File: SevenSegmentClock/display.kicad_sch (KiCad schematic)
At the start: 86 parts, among them Q1 PN2222A, Q2 PN2222A, Q3 PN2222A, Q4 PN2222A, U1 4504, U10 4511, U2 74HC138, U3 4504, U4 4042, U5 4511, U6 4511, U7 4511, U8 4511, U9 4511

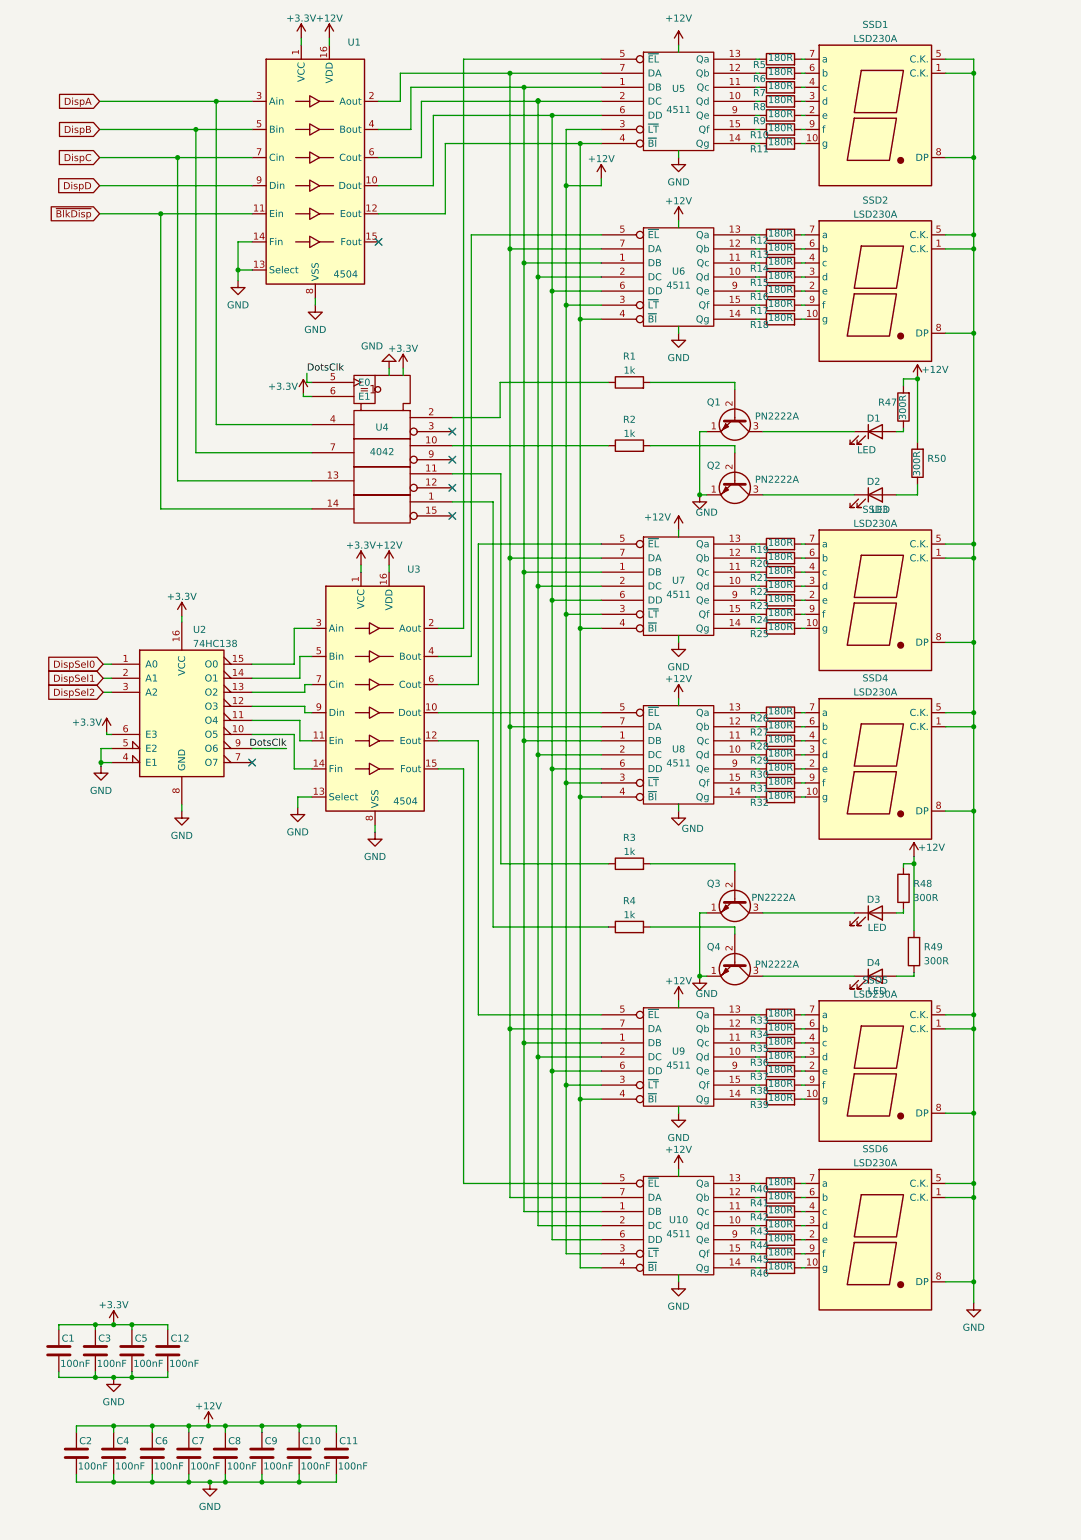
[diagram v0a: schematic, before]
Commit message: Using SigmaDelta to implement dimming of the display
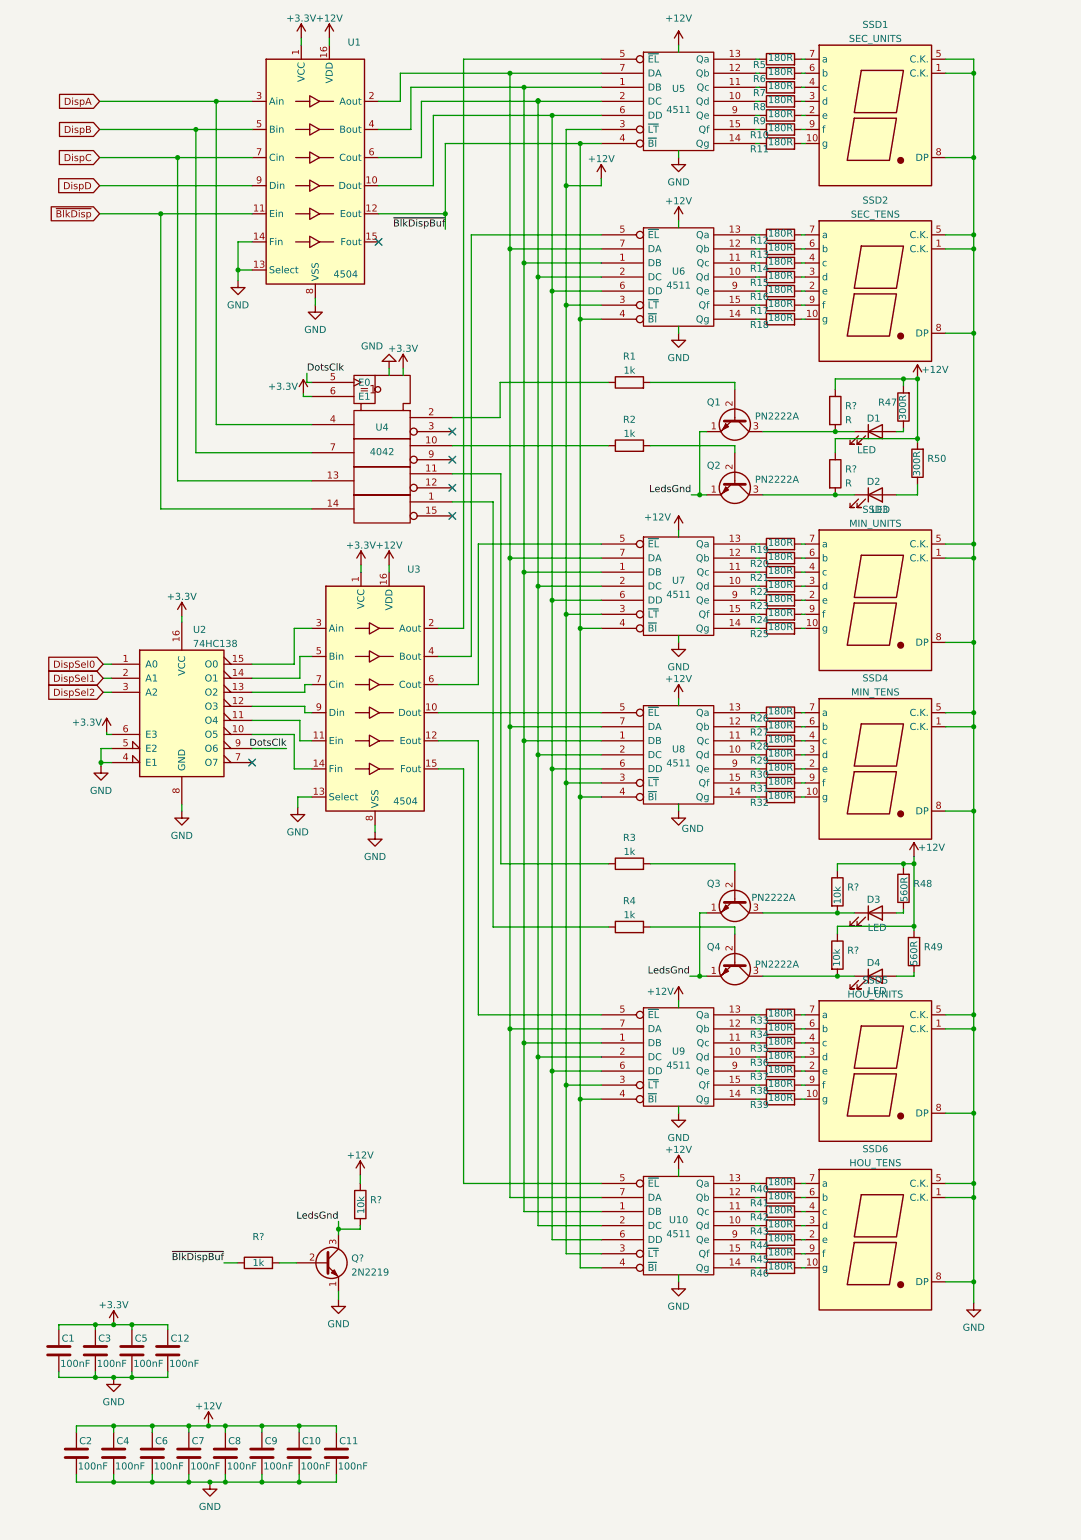
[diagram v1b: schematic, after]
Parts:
- added Q?: 2N2219, Package_TO_SOT_THT:TO-39-3, symbol Transistor_BJT:2N2219
- added R? (x3): 10k, symbol Device:R
- added R? (x2): R, symbol Device:R
- added R?: 1k, symbol Device:R
- R48, R49: value 300R -> 560R
- SSD1: value LSD230A -> SEC_UNITS
- SSD2: value LSD230A -> SEC_TENS
- SSD3: value LSD230A -> MIN_UNITS
- SSD4: value LSD230A -> MIN_TENS
- SSD5: value LSD230A -> HOU_UNITS
- SSD6: value LSD230A -> HOU_TENS
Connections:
- net +12V: now also R?.1, R?.1, R?.1, R?.1, R?.1
- net GND: now also Q?.1 (E); no longer Q1.1 (E), Q2.1 (E), Q3.1 (E), Q4.1 (E)
- net at D2.1 (K), Q2.3 (C): now also R?.2
- net at D1.1 (K), Q1.3 (C): now also R?.2
- net at D3.1 (K), Q3.3 (C): now also R?.2
- net ~{BlkDispBuf}: now reaches U1.12 (Eout), U10.4 (~{BI}), U5.4 (~{BI}), U6.4 (~{BI}), U7.4 (~{BI}), U8.4 (~{BI}), U9.4 (~{BI})
- net ~{BlkDispBuf}: now also R?.1
- net at D4.1 (K), Q4.3 (C): now also R?.2
- new net: Q?.2 (B), R?.2
- new net LedsGnd: Q1.1 (E), Q2.1 (E), Q3.1 (E), Q4.1 (E), Q?.3 (C), R?.2

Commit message: Adding two more displays to show a degree and a percent symbols
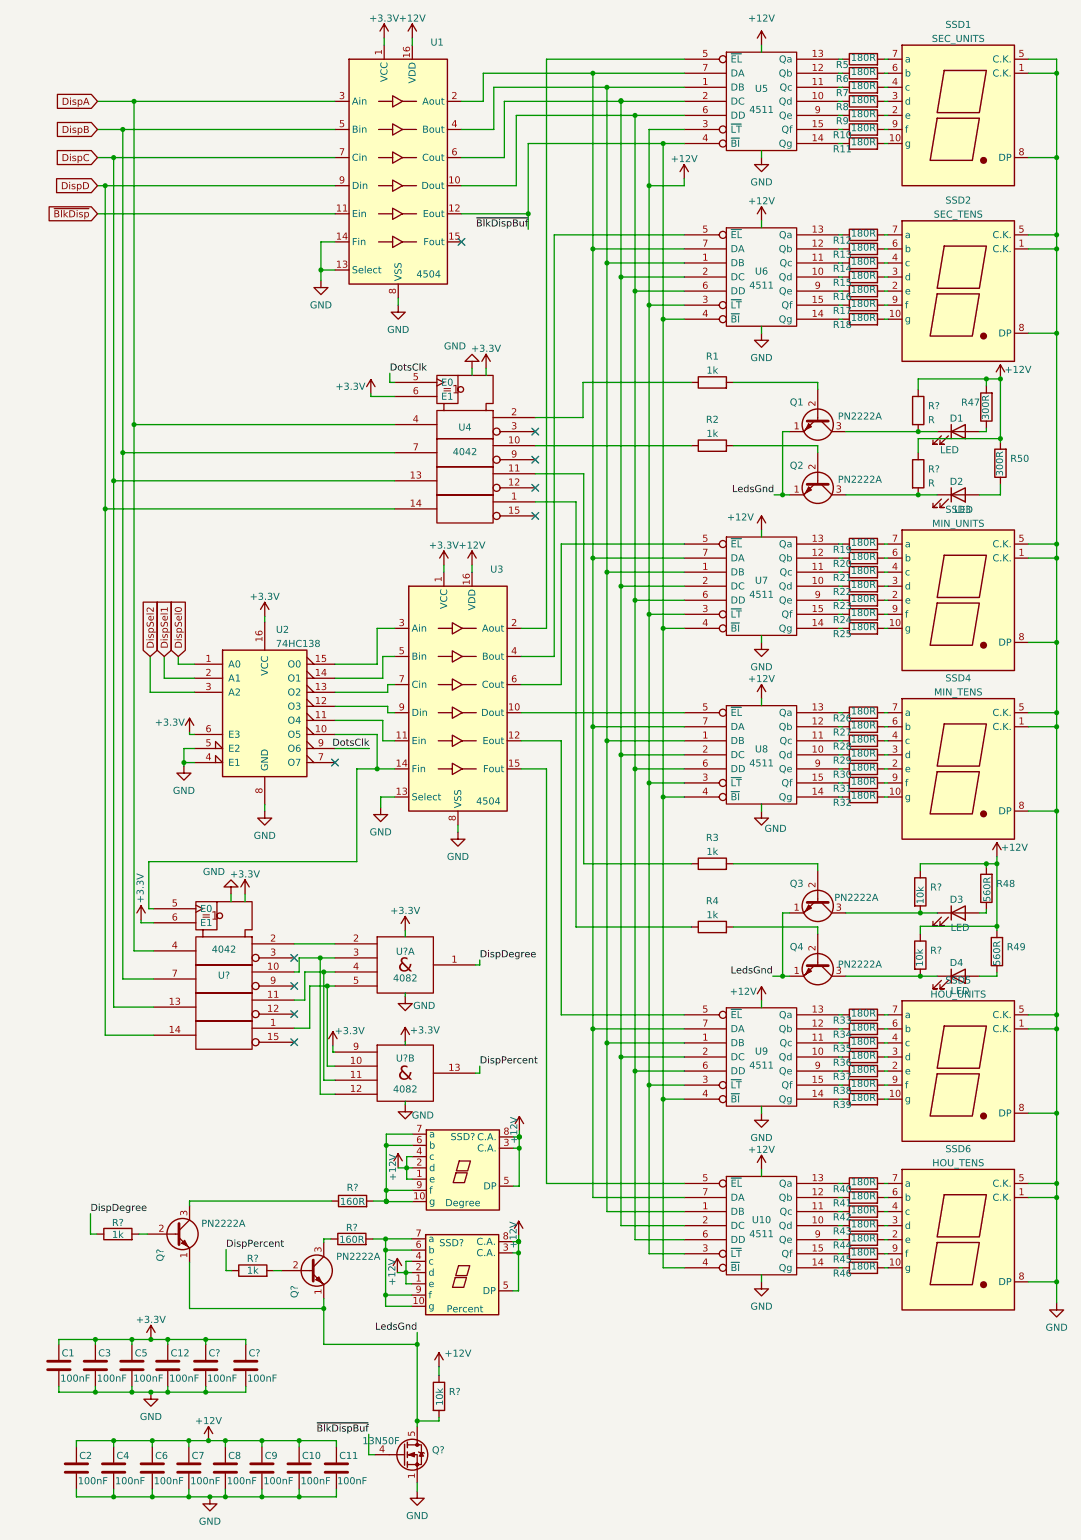
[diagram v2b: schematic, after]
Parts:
- removed Q?: 2N2219, Package_TO_SOT_THT:TO-39-3, symbol Transistor_BJT:2N2219
- removed R?: 1k, symbol Device:R
- added C? (x2): 100nF, Capacitor_THT:C_Disc_D5.0mm_W2.5mm_P5.00mm, symbol Device:C
- added Q? (x2): PN2222A, Package_TO_SOT_THT:TO-92_Inline, symbol Transistor_BJT:PN2222A
- added Q?: 13N50F, Package_TO_SOT_SMD:LFPAK33, symbol Transistor_FET:BUK7M67-60EX
- added R? (x2): 1k, symbol Device:R
- added R? (x2): 160R, symbol Device:R
- added SSD?: Degree, symbol Library:WCN1-1056
- added SSD?: Percent, symbol Library:WCN1-1056
- added U? (x2): 4082, symbol 4xxx_IEEE:4082
- added U?: 4042, symbol 4xxx_IEEE:4042
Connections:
- net +12V: now also C?.1, C?.1, SSD?.1 (e), SSD?.1 (e), SSD?.2 (d), SSD?.2 (d), SSD?.3 (C.A.), SSD?.3 (C.A.), SSD?.4 (c), SSD?.4 (c), SSD?.5 (DP), SSD?.5 (DP), SSD?.8 (C.A.), SSD?.8 (C.A.), U?.14 (Vdd), U?.14 (Vdd), U?.16 (Vdd), U?.6 (E1), U?.9
- net DispA: now also U?.4
- net DispB: now also U?.7
- net DispC: now also U?.13
- net DispD: now also U4.14, U?.14
- net GND: now also C?.2, C?.2, Q?.1 (S), Q?.2 (S), Q?.3 (S), U?.7 (Vss), U?.7 (Vss), U?.8 (Vss)
- net LedsGnd: now also Q?.1 (E), Q?.1 (E), Q?.5 (D)
- net ~{BlkDispBuf}: now also Q?.4 (G)
- net ~{BlkDisp}: no longer U4.14
- net at U2.10 (O5), U3.14 (Fin): now also U?.5 (E0)
- new net: U?.2, U?.2
- new net: U?.10, U?.12, U?.3
- new net: U?.11, U?.11, U?.4
- new net: U?.1, U?.10, U?.5
- new net: Q?.2 (B), R?.2 (x2)
- new net: Q?.3 (C), R?.1 (x2)
- new net: R?.2, SSD?.10 (g), SSD?.6 (b), SSD?.7 (a), SSD?.9 (f) (x2)
- new net DispDegree: R?.1, U?.1
- new net DispPercent: R?.1, U?.13
- no-connect marks 6 -> 10
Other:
- moved on the sheet: C1, C10, C11, C12, C2, C3, C4, C5, C6, C7, C8, C9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

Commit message: Adding the control schematic and fixing Eletrical Rules Checks
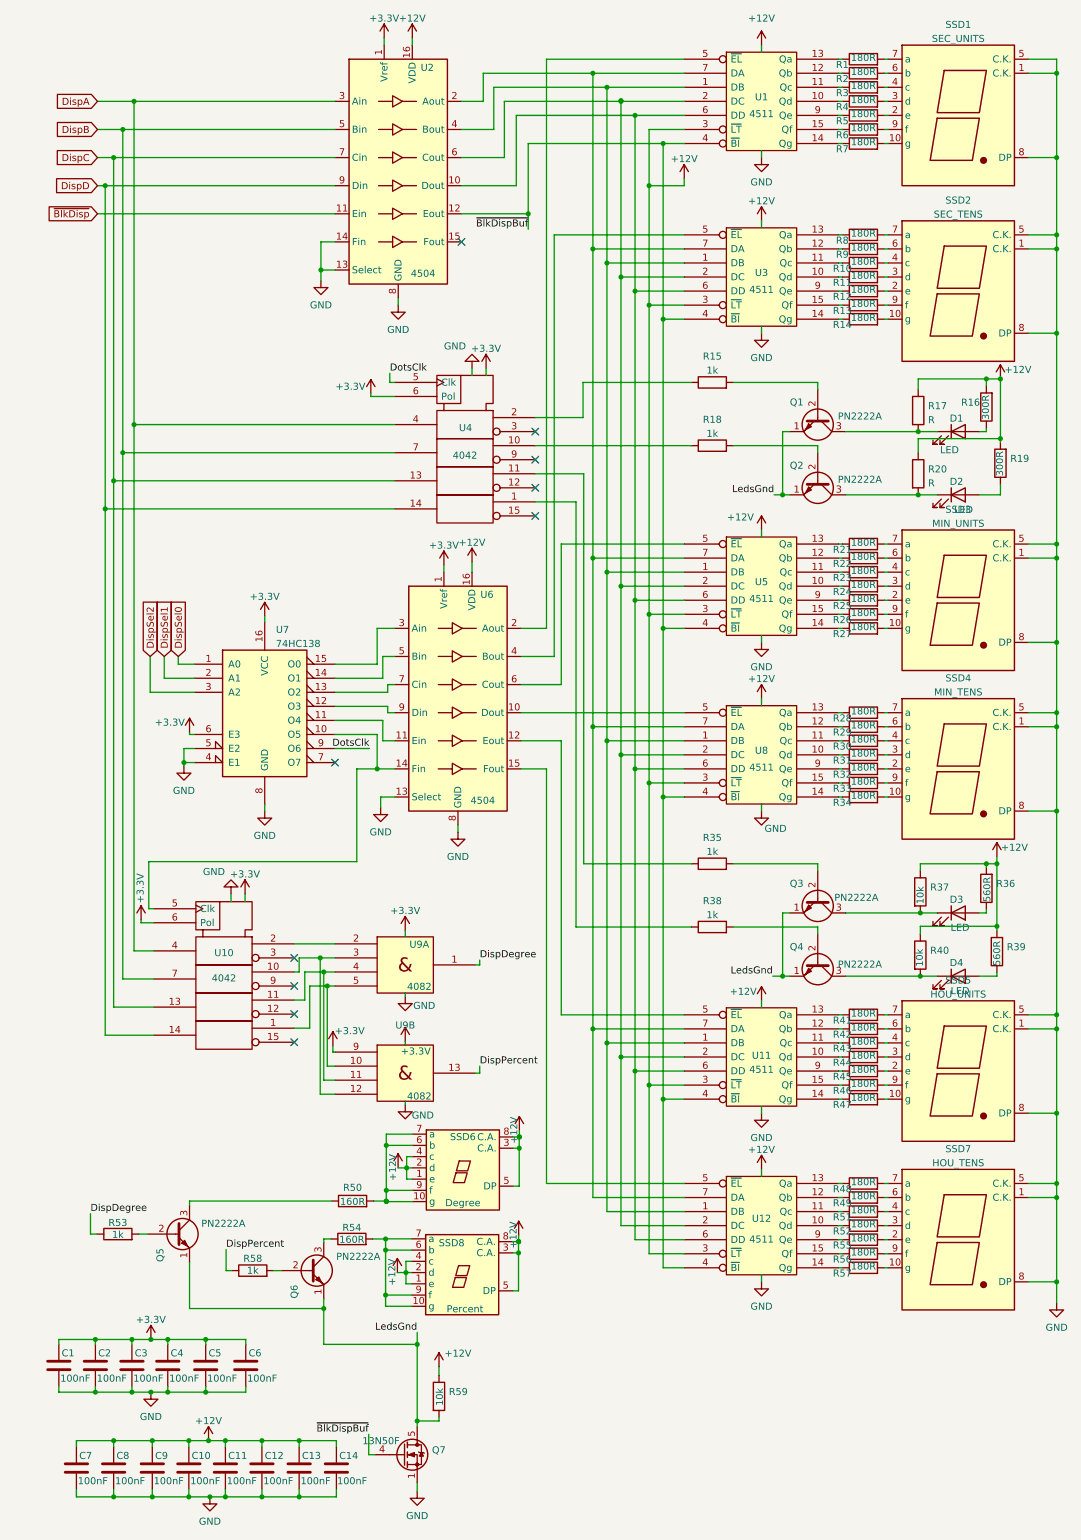
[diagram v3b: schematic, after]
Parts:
- removed U1, U3: 4504, Package_SO:SOIC-16_3.9x9.9mm_P1.27mm, symbol 4xxx:4504
- removed U10, U5, U6, U7, U8, U9: 4511, Package_SO:SOIC-16_3.9x9.9mm_P1.27mm, symbol 4xxx_IEEE:4511
- removed U4: 4042, Package_DIP:DIP-16_W7.62mm_LongPads, symbol 4xxx_IEEE:4042
- removed U? (x2): 4082, symbol 4xxx_IEEE:4082
- removed U?: 4042, symbol 4xxx_IEEE:4042
- added U1, U11, U12, U3, U5, U8: 4511, symbol Library:4511
- added U10, U4: 4042, symbol Library:4042
- added U2, U6: 4504, symbol Library:4504
- added U9: 4082, symbol Library:4082
- gave numbers to parts that had none: 16
- renumbered C7 to C10, C8 to C11, C9 to C12, C10 to C13, C11 to C14, C3 to C2, C5 to C3, C12 to C4, C2 to C7, C4 to C8, C6 to C9, R5 to R1, R14 to R10, R15 to R11, R16 to R12, R17 to R13, R18 to R14, R1 to R15, R47 to R16, R2 to R18, R50 to R19, R6 to R2, R19 to R21, R20 to R22, R21 to R23, R22 to R24, R23 to R25, R24 to R26, R25 to R27, R26 to R28, R27 to R29, R7 to R3, R28 to R30, R29 to R31, R30 to R32, R31 to R33, R32 to R34, R3 to R35, R48 to R36, R4 to R38, R49 to R39, R8 to R4, R33 to R41, R34 to R42, R35 to R43, R36 to R44, R37 to R45, R38 to R46, R39 to R47, R40 to R48, R41 to R49, R9 to R5, R42 to R51, R43 to R52, R44 to R55, R45 to R56, R46 to R57, R10 to R6, R11 to R7, R12 to R8, R13 to R9, SSD6 to SSD7, U2 to U7
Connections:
- net +12V: now also U1.16 (Vdd), U1.3 (~{LT}), U11.16 (Vdd), U11.3 (~{LT}), U12.16 (Vdd), U12.3 (~{LT}), U2.16 (VDD), U3.16 (Vdd), U3.3 (~{LT}), U5.16 (Vdd), U5.3 (~{LT}), U6.16 (VDD), U8.16 (Vdd), U8.3 (~{LT}); no longer C1.1, C2.1, C3.1, C4.1, C5.1, C6.1, U7.16 (VCC), U7.6 (E3)
- net DispA: now also U10.4, U2.3 (Ain), U4.4
- net DispB: now also U10.7, U2.5 (Bin), U4.7
- net DispC: now also U10.13, U2.7 (Cin), U4.13
- net DispD: now also U10.14, U2.9 (Din), U4.14
- net DispDegree: now also U9.1
- net DispPercent: now also U9.13
- net DotsClk: now also U4.5 (Clk)
- net GND: now also U1.8 (GND), U10.8 (GND), U11.8 (GND), U12.8 (GND), U2.13 (Select), U2.14 (Fin), U2.8 (GND), U3.8 (GND), U4.8 (GND), U5.8 (GND), U6.13 (Select), U6.8 (GND), U8.8 (GND), U9.7 (GND), U9.7 (GND)
- net ~{BlkDispBuf}: now also U1.4 (~{BI}), U11.4 (~{BI}), U12.4 (~{BI}), U2.12 (Eout), U3.4 (~{BI}), U5.4 (~{BI}), U8.4 (~{BI})
- net ~{BlkDisp}: now also U2.11 (Ein)
- net at R18.1: now also U4.10
- net at R30.1: now also U8.11 (Qc)
- net at R52.1: now also U12.10 (Qd)
- net at R28.1: now also U8.13 (Qa)
- net at R41.1: now also U11.13 (Qa)
- net at R32.1: now also U8.9 (Qe)
- net at R11.1: now also U3.10 (Qd)
- net at R10.1: now also U3.11 (Qc)
- net at R9.1: now also U3.12 (Qb)
- net at R8.1: now also U3.13 (Qa)
- net at R14.1: now also U3.14 (Qg)
- net at R13.1: now also U3.15 (Qf)
- net at R12.1: now also U3.9 (Qe)
- net at R44.1: now also U11.10 (Qd)
- net at R43.1: now also U11.11 (Qc)
- net at R42.1: now also U11.12 (Qb)
- net at R47.1: now also U11.14 (Qg)
- net at R46.1: now also U11.15 (Qf)
- net at R45.1: now also U11.9 (Qe)
- net at R24.1: now also U5.10 (Qd)
- net at R29.1: now also U8.12 (Qb)
- net at R21.1: now also U5.13 (Qa)
- net at U7.11 (O4): now also U6.11 (Ein)
- net at U7.10 (O5): now also U10.5 (Clk), U6.14 (Fin)
- net at U7.15 (O0): now also U6.3 (Ain)
- net at U7.14 (O1): now also U6.5 (Bin)
- net at U7.13 (O2): now also U6.7 (Cin)
- net at U7.12 (O3): now also U6.9 (Din)
- net at R7.1: now also U1.14 (Qg)
- net at R26.1: now also U5.15 (Qf)
- net at R31.1: now also U8.10 (Qd)
- net at R34.1: now also U8.14 (Qg)
- net at R33.1: now also U8.15 (Qf)
- net at R48.1: now also U12.13 (Qa)
- net at R23.1: now also U5.11 (Qc)
- net at R38.1: now also U4.1
- net at R35.1: now also U4.11
- net at R15.1: now also U4.2
- net at R3.1: now also U1.11 (Qc)
- net at R1.1: now also U1.13 (Qa)
- net at R6.1: now also U1.15 (Qf)
- net at R4.1: now also U1.10 (Qd)
- net at R2.1: now also U1.12 (Qb)
- net at R5.1: now also U1.9 (Qe)
- net at R56.1: now also U12.15 (Qf)
- net at R25.1: now also U5.9 (Qe)
- net at R51.1: now also U12.11 (Qc)
- net at R49.1: now also U12.12 (Qb)
- net at R57.1: now also U12.14 (Qg)
- net at R55.1: now also U12.9 (Qe)
- net at R22.1: now also U5.12 (Qb)
- net at R27.1: now also U5.14 (Qg)
- new net: U1.1 (DB), U11.1 (DB), U12.1 (DB), U2.4 (Bout), U3.1 (DB), U5.1 (DB), U8.1 (DB)
- new net: U1.2 (DC), U11.2 (DC), U12.2 (DC), U2.6 (Cout), U3.2 (DC), U5.2 (DC), U8.2 (DC)
- new net: U1.5 (~{EL}), U6.2 (Aout)
- new net: U1.6 (DD), U11.6 (DD), U12.6 (DD), U2.10 (Dout), U3.6 (DD), U5.6 (DD), U8.6 (DD)
- new net: U1.7 (DA), U11.7 (DA), U12.7 (DA), U2.2 (Aout), U3.7 (DA), U5.7 (DA), U8.7 (DA)
- new net: U10.1, U9.10, U9.5
- new net: U10.10, U9.12, U9.3
- new net: U10.11, U9.11, U9.4
- new net: U10.2, U9.2
- new net: U6.10 (Dout), U8.5 (~{EL})
- new net: U5.5 (~{EL}), U6.6 (Cout)
- new net: U3.5 (~{EL}), U6.4 (Bout)
- new net: U11.5 (~{EL}), U6.12 (Eout)
- new net: U12.5 (~{EL}), U6.15 (Fout)
- new net +3.3V: C1.1, C2.1, C3.1, C4.1, C5.1, C6.1, U10.16 (Vcc), U10.6 (Pol), U2.1 (Vref), U4.16 (Vcc), U4.6 (Pol), U6.1 (Vref), U7.16 (VCC), U7.6 (E3), U9.14 (Vcc), U9.14 (Vcc), U9.9

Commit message: Assigning footprints
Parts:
- removed Q7: 13N50F, Package_TO_SOT_SMD:LFPAK33, symbol Transistor_FET:BUK7M67-60EX
- added Q7: 13N50F, Package_TO_SOT_THT:TO-220-3_Vertical, symbol Library:SVD13N50F
- R1, R10, R11, R12, R13, R14, R2, R21, R22, R23, R24, R25, R26, R27, R28, R29, R3, R30, R31, R32, R33, R34, R4, R41, R42, R43, R44, R45, R46, R47, R48, R49, R5, R51, R52, R55, R56, R57, R6, R7, R8, R9: value 180R -> 160R; footprint Resistor_THT:R_Axial_DIN0207_L6.3mm_D2.5mm_P7.62mm_Horizontal -> Resistor_SMD:R_1206_3216Metric_Pad1.30x1.75mm_HandSolder
- R15, R18, R35, R36, R38, R39: footprint Resistor_THT:R_Axial_DIN0207_L6.3mm_D2.5mm_P7.62mm_Horizontal -> Resistor_SMD:R_1206_3216Metric_Pad1.30x1.75mm_HandSolder
- R16, R19: value 300R -> 560R; footprint Resistor_THT:R_Axial_DIN0207_L6.3mm_D2.5mm_P7.62mm_Horizontal -> Resistor_SMD:R_1206_3216Metric_Pad1.30x1.75mm_HandSolder
- R17, R20: value R -> 10k; footprint (none) -> Resistor_THT:R_Axial_DIN0207_L6.3mm_D2.5mm_P10.16mm_Horizontal
- R37, R40, R59: footprint (none) -> Resistor_THT:R_Axial_DIN0207_L6.3mm_D2.5mm_P10.16mm_Horizontal
- R50, R53, R54, R58: footprint (none) -> Resistor_SMD:R_1206_3216Metric_Pad1.30x1.75mm_HandSolder
- SSD6, SSD8: footprint (none) -> Display_7Segment:7SegmentLED_LTS6760_LTS6780
- U1, U11, U12, U2, U3, U5, U6, U8: footprint (none) -> Package_SO:SOIC-16W_5.3x10.2mm_P1.27mm
- U10, U4: footprint (none) -> Package_DIP:DIP-16_W7.62mm_Socket_LongPads
- U9: footprint (none) -> Package_DIP:DIP-14_W7.62mm_Socket_LongPads
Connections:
- net GND: now also Q7.3 (S)
- net LedsGnd: now also Q7.2 (D)
- net ~{BlkDispBuf}: now also Q7.1 (G)
